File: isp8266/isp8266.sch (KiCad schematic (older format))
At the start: 70 parts, among them J1 S0, J10 9V_IN, J11 USB_C_Receptacle, J12 F1, J2 S2, J3 S1, J4 S3, J5 IMU, J6 USART, J7 F0, J8 BATTERY, J9 I2C, Q1 S8050, Q2 S8050, Q3 BSS138, Q4 IRLML6402, Q5 BSS138, Q6 IRLML6402, U1 CH340C, U2 AP1117-33, U3 IP5306, U4 ESP-12E

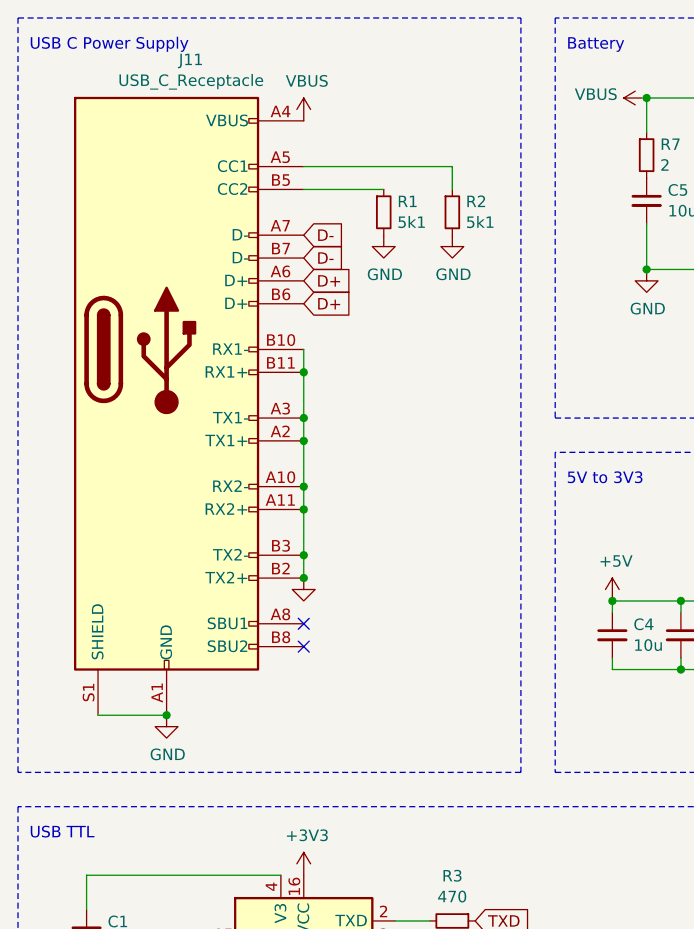
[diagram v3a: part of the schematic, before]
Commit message: Change usb c connector
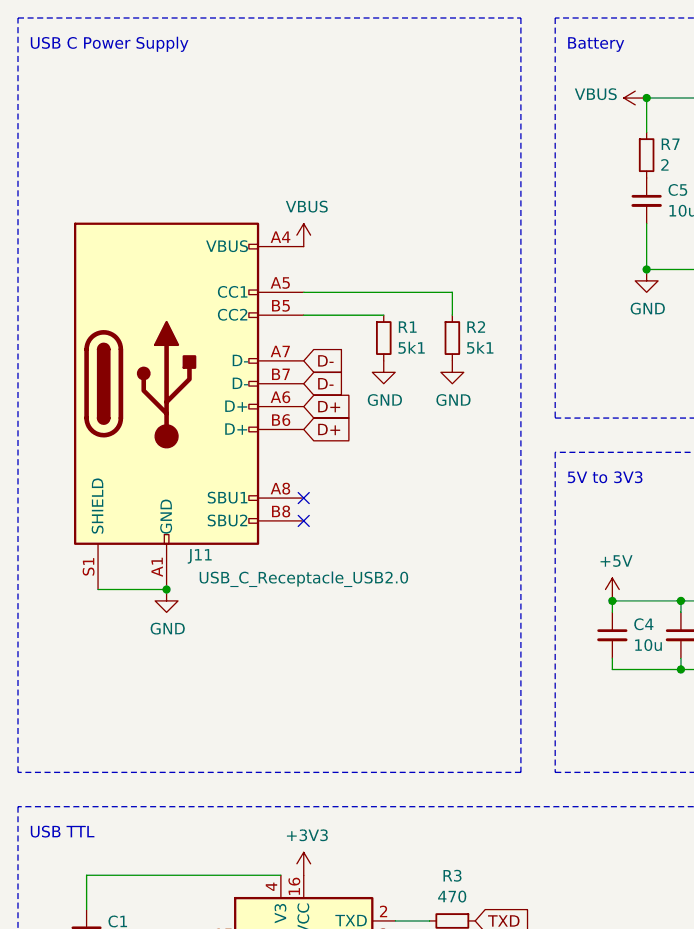
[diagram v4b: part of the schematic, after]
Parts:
- removed J11: USB_C_Receptacle, Connector_USB:USB_C_Receptacle_Amphenol_12401610E4-2A, symbol Connector:USB_C_Receptacle
- added J11: USB_C_Receptacle_USB2.0, Connector_USB:USB_C_Receptacle_Palconn_UTC16-G, symbol Connector:USB_C_Receptacle_USB2.0
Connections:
- net -BATT: now also J11.A1 (GND), J11.A12 (GND), J11.B1 (GND), J11.B12 (GND), J11.S1 (SHIELD)
- net D+: now also J11.A6 (D+), J11.B6 (D+)
- net D-: now also J11.A7 (D-), J11.B7 (D-)
- net VBUS: now also J11.A4 (VBUS), J11.A9 (VBUS), J11.B4 (VBUS), J11.B9 (VBUS)
- net at R1.1: now also J11.B5 (CC2)
- net at R2.1: now also J11.A5 (CC1)
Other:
- moved on the sheet: R1, R2
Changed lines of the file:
@@
 Comment4 ""
 $EndDescr
-Text GLabel 1900 1750 2    50   Input ~ 0
+Text GLabel 1900 2300 2    50   Input ~ 0
 D+
-Text GLabel 1900 1550 2    50   Input ~ 0
+Text GLabel 1900 2100 2    50   Input ~ 0
 D-
-Wire Wire Line
-	1000 3650 1300 3650
-$Comp
-L power:GND #PWR04
-U 1 1 638110D1
-P 1300 3650
-F 0 "#PWR04" H 1300 3400 50  0001 C CNN
-F 1 "GND" H 1305 3477 50  0000 C CNN
-F 2 "" H 1300 3650 50  0001 C CNN
-F 3 "" H 1300 3650 50  0001 C CNN
-	1    1300 3650
-	1    0    0    -1
-$EndComp
 $Comp
 L Device:R_Small R1
 U 1 1 63811A2A
-P 2250 1450
-F 0 "R1" H 2309 1496 50  0000 L CNN
-F 1 "5k1" H 2309 1405 50  0000 L CNN
-F 2 "Resistor_SMD:R_0603_1608Metric" H 2250 1450 50  0001 C CNN
-F 3 "~" H 2250 1450 50  0001 C CNN
-	1    2250 1450
+P 2250 2000
+F 0 "R1" H 2309 2046 50  0000 L CNN
+F 1 "5k1" H 2309 1955 50  0000 L CNN
+F 2 "Resistor_SMD:R_0603_1608Metric" H 2250 2000 50  0001 C CNN
+F 3 "~" H 2250 2000 50  0001 C CNN
+	1    2250 2000
 	1    0    0    -1
 $EndComp
@@
 L Device:R_Small R2
 U 1 1 63813179
-P 2550 1450
-F 0 "R2" H 2609 1496 50  0000 L CNN
-F 1 "5k1" H 2609 1405 50  0000 L CNN
-F 2 "Resistor_SMD:R_0603_1608Metric" H 2550 1450 50  0001 C CNN
-F 3 "~" H 2550 1450 50  0001 C CNN
-	1    2550 1450
-	1    0    0    -1
-$EndComp
-Wire Wire Line
-	2550 1350 2550 1250
-Wire Wire Line
-	2550 1250 1900 1250
-Wire Wire Line
-	1900 1350 2250 1350
+P 2550 2000
+F 0 "R2" H 2609 2046 50  0000 L CNN
+F 1 "5k1" H 2609 1955 50  0000 L CNN
+F 2 "Resistor_SMD:R_0603_1608Metric" H 2550 2000 50  0001 C CNN
+F 3 "~" H 2550 2000 50  0001 C CNN
+	1    2550 2000
+	1    0    0    -1
+$EndComp
+Wire Wire Line
+	2550 1900 2550 1800
+Wire Wire Line
+	2550 1800 1900 1800
+Wire Wire Line
+	1900 1900 2250 1900
 $Comp
 L power:GND #PWR09
 U 1 1 638144D3
-P 2250 1550
-F 0 "#PWR09" H 2250 1300 50  0001 C CNN
-F 1 "GND" H 2255 1377 50  0000 C CNN
-F 2 "" H 2250 1550 50  0001 C CNN
-F 3 "" H 2250 1550 50  0001 C CNN
-	1    2250 1550
+P 2250 2100
+F 0 "#PWR09" H 2250 1850 50  0001 C CNN
+F 1 "GND" H 2255 1927 50  0000 C CNN
+F 2 "" H 2250 2100 50  0001 C CNN
+F 3 "" H 2250 2100 50  0001 C CNN
+	1    2250 2100
 	1    0    0    -1
 $EndComp
@@
 L power:GND #PWR010
 U 1 1 63814BDE
-P 2550 1550
-F 0 "#PWR010" H 2550 1300 50  0001 C CNN
-F 1 "GND" H 2555 1377 50  0000 C CNN
-F 2 "" H 2550 1550 50  0001 C CNN
-F 3 "" H 2550 1550 50  0001 C CNN
-	1    2550 1550
-	1    0    0    -1
-$EndComp
-$Comp
-L power:GND #PWR06
-U 1 1 63815628
-P 1900 3050
-F 0 "#PWR06" H 1900 2800 50  0001 C CNN
-F 1 "GND" H 1905 2877 50  0001 C CNN
-F 2 "" H 1900 3050 50  0001 C CNN
-F 3 "" H 1900 3050 50  0001 C CNN
-	1    1900 3050
-	1    0    0    -1
-$EndComp
-NoConn ~ 1900 3250
-NoConn ~ 1900 3350
+P 2550 2100
+F 0 "#PWR010" H 2550 1850 50  0001 C CNN
+F 1 "GND" H 2555 1927 50  0000 C CNN
+F 2 "" H 2550 2100 50  0001 C CNN
+F 3 "" H 2550 2100 50  0001 C CNN
+	1    2550 2100
+	1    0    0    -1
+$EndComp
 $Comp
 L power:VBUS #PWR05
 U 1 1 63834DD7
-P 1900 1050
-F 0 "#PWR05" H 1900 900 50  0001 C CNN
-F 1 "VBUS" H 1915 1223 50  0000 C CNN
-F 2 "" H 1900 1050 50  0001 C CNN
-F 3 "" H 1900 1050 50  0001 C CNN
-	1    1900 1050
+P 1900 1600
+F 0 "#PWR05" H 1900 1450 50  0001 C CNN
+F 1 "VBUS" H 1915 1773 50  0000 C CNN
+F 2 "" H 1900 1600 50  0001 C CNN
+F 3 "" H 1900 1600 50  0001 C CNN
+	1    1900 1600
 	1    0    0    -1
 $EndComp
@@
 	1    0    0    -1
 $EndComp
-$Comp
-L Connector:USB_C_Receptacle J11
-U 1 1 63C95E22
-P 1300 2050
-F 0 "J11" H 1407 3317 50  0000 C CNN
-F 1 "USB_C_Receptacle" H 1407 3226 50  0000 C CNN
-F 2 "Connector_USB:USB_C_Receptacle_Amphenol_12401610E4-2A" H 1450 2050 50  0001 C CNN
-F 3 "https://www.usb.org/sites/default/files/documents/usb_type-c.zip" H 1450 2050 50  0001 C CNN
-	1    1300 2050
-	1    0    0    -1
-$EndComp
-Connection ~ 1300 3650
-Wire Wire Line
-	1900 2950 1900 3050
-Connection ~ 1900 3050
-Wire Wire Line
-	1900 2050 1900 2150
-Connection ~ 1900 2150
-Wire Wire Line
-	1900 2150 1900 2350
-Connection ~ 1900 2350
-Wire Wire Line
-	1900 2350 1900 2450
-Connection ~ 1900 2450
-Wire Wire Line
-	1900 2450 1900 2650
-Connection ~ 1900 2650
-Wire Wire Line
-	1900 2650 1900 2750
-Connection ~ 1900 2750
-Wire Wire Line
-	1900 2750 1900 2950
-Connection ~ 1900 2950
-Text GLabel 1900 1650 2    50   Input ~ 0
-D-
-Text GLabel 1900 1850 2    50   Input ~ 0
-D+
 Wire Notes Line
 	3000 3900 5650 3900
@@
 $EndComp
 Connection ~ 8850 5050
+Text GLabel 1900 2400 2    50   Input ~ 0
+D+
+Text GLabel 1900 2200 2    50   Input ~ 0
+D-
+Wire Wire Line
+	1000 3100 1300 3100
+$Comp
+L power:GND #PWR04
+U 1 1 638110D1
+P 1300 3100
+F 0 "#PWR04" H 1300 2850 50  0001 C CNN
+F 1 "GND" H 1305 2927 50  0000 C CNN
+F 2 "" H 1300 3100 50  0001 C CNN
+F 3 "" H 1300 3100 50  0001 C CNN
+	1    1300 3100
+	1    0    0    -1
+$EndComp
+Connection ~ 1300 3100
+$Comp
+L Connector:USB_C_Receptacle_USB2.0 J11
+U 1 1 63983D7F
+P 1300 2200
+F 0 "J11" H 1450 1450 50  0000 C CNN
+F 1 "USB_C_Receptacle_USB2.0" H 1900 1350 50  0000 C CNN
+F 2 "Connector_USB:USB_C_Receptacle_Palconn_UTC16-G" H 1450 2200 50  0001 C CNN
+F 3 "https://www.usb.org/sites/default/files/documents/usb_type-c.zip" H 1450 2200 50  0001 C CNN
+	1    1300 2200
+	1    0    0    -1
+$EndComp
+NoConn ~ 1900 2800
+NoConn ~ 1900 2700
 $EndSCHEMATC

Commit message: Edit BJT footprint
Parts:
- Q1, Q2: footprint Package_TO_SOT_THT:TO-92_Inline -> Package_TO_SOT_SMD:SOT-23
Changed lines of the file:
@@
 F 0 "Q1" H 3541 5046 50  0000 L CNN
 F 1 "S8050" H 3541 4955 50  0000 L CNN
-F 2 "Package_TO_SOT_THT:TO-92_Inline" H 3550 4925 50  0001 L CIN
+F 2 "Package_TO_SOT_SMD:SOT-23" H 3550 4925 50  0001 L CIN
 F 3 "http://www.unisonic.com.tw/datasheet/S8050.pdf" H 3350 5000 50  0001 L CNN
 	1    3350 5000
@@
 F 0 "Q2" H 3541 5404 50  0000 L CNN
 F 1 "S8050" H 3541 5495 50  0000 L CNN
-F 2 "Package_TO_SOT_THT:TO-92_Inline" H 3550 5375 50  0001 L CIN
+F 2 "Package_TO_SOT_SMD:SOT-23" H 3550 5375 50  0001 L CIN
 F 3 "http://www.unisonic.com.tw/datasheet/S8050.pdf" H 3350 5450 50  0001 L CNN
 	1    3350 5450

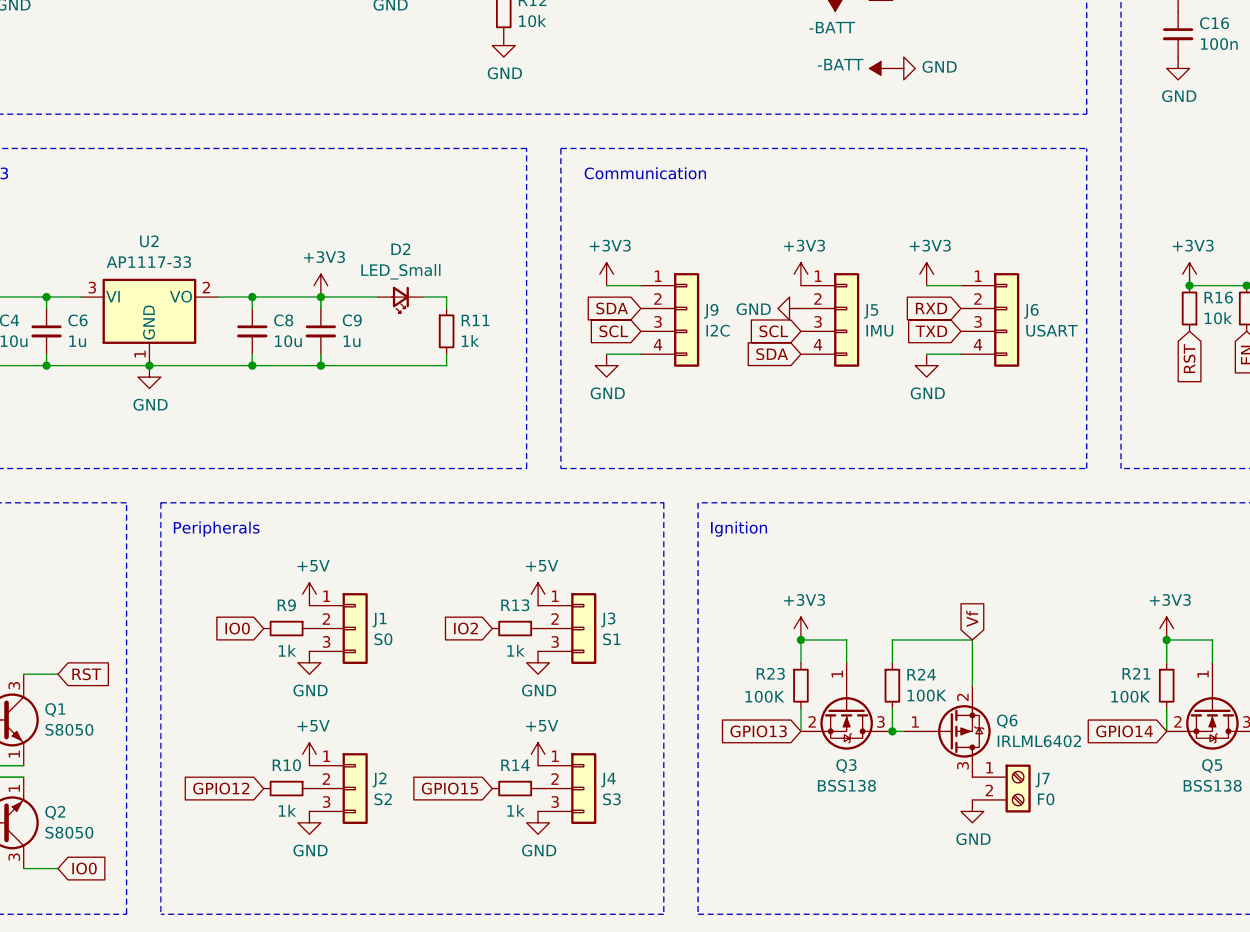
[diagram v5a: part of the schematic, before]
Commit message: Change pinout connector
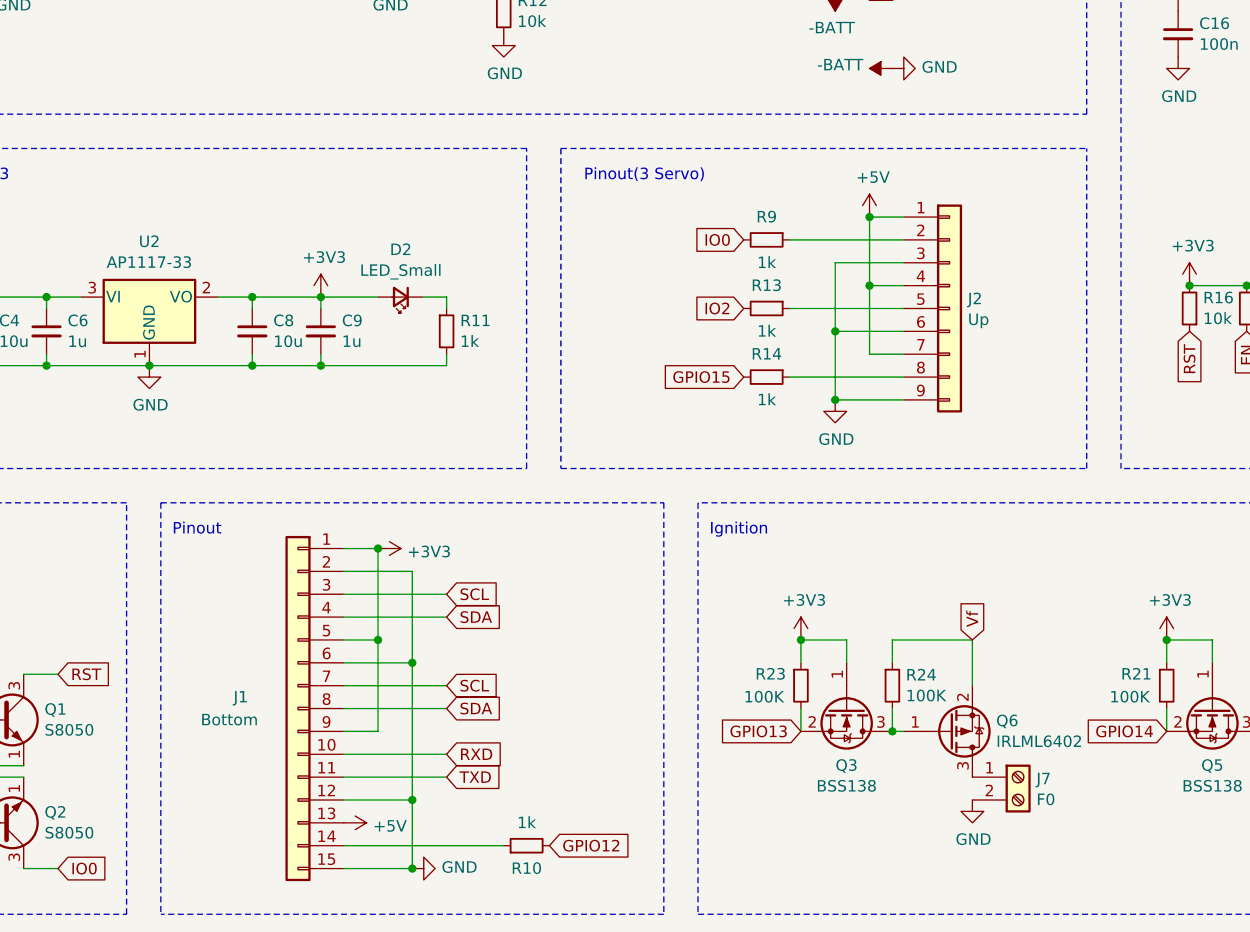
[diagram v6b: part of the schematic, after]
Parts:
- removed J1: S0, Connector_PinSocket_2.54mm:PinSocket_1x03_P2.54mm_Vertical, symbol Connector_Generic:Conn_01x03
- removed J2: S2, Connector_PinSocket_2.54mm:PinSocket_1x03_P2.54mm_Vertical, symbol Connector_Generic:Conn_01x03
- removed J3: S1, Connector_PinSocket_2.54mm:PinSocket_1x03_P2.54mm_Vertical, symbol Connector_Generic:Conn_01x03
- removed J4: S3, Connector_PinSocket_2.54mm:PinSocket_1x03_P2.54mm_Vertical, symbol Connector_Generic:Conn_01x03
- removed J5: IMU, Connector_PinSocket_2.54mm:PinSocket_1x04_P2.54mm_Vertical, symbol Connector_Generic:Conn_01x04
- removed J6: USART, Connector_PinSocket_2.54mm:PinSocket_1x04_P2.54mm_Vertical, symbol Connector_Generic:Conn_01x04
- removed J9: I2C, Connector_PinSocket_2.54mm:PinSocket_1x04_P2.54mm_Vertical, symbol Connector_Generic:Conn_01x04
- added J1: Bottom, Connector_PinHeader_2.54mm:PinHeader_1x15_P2.54mm_Vertical, symbol Connector_Generic:Conn_01x15
- added J2: Up, Connector_PinHeader_2.54mm:PinHeader_1x09_P2.54mm_Vertical, symbol Connector_Generic:Conn_01x09
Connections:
- net +3V3: now also J1.1 (Pin_1), J1.5 (Pin_5), J1.9 (Pin_9)
- net +5V: now also J1.13 (Pin_13), J2.1 (Pin_1), J2.4 (Pin_4), J2.7 (Pin_7)
- net -BATT: now also J1.12 (Pin_12), J1.15 (Pin_15), J1.2 (Pin_2), J1.6 (Pin_6), J2.3 (Pin_3), J2.6 (Pin_6), J2.9 (Pin_9)
- net RXD: now also J1.10 (Pin_10)
- net SCL: now also J1.3 (Pin_3), J1.7 (Pin_7)
- net SDA: now also J1.4 (Pin_4), J1.8 (Pin_8)
- net TXD: now also J1.11 (Pin_11)
- net at R9.1: now also J2.2 (Pin_2)
- net at R13.1: now also J2.5 (Pin_5)
- net at R10.1: now also J1.14 (Pin_14)
- net at R14.1: now also J2.8 (Pin_8)
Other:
- note added: "Pinout"
- note added: "Pinout(3 Servo)"
- note removed: "Communication"
- note removed: "Peripherals"
- moved on the sheet: R10, R13, R14, R9

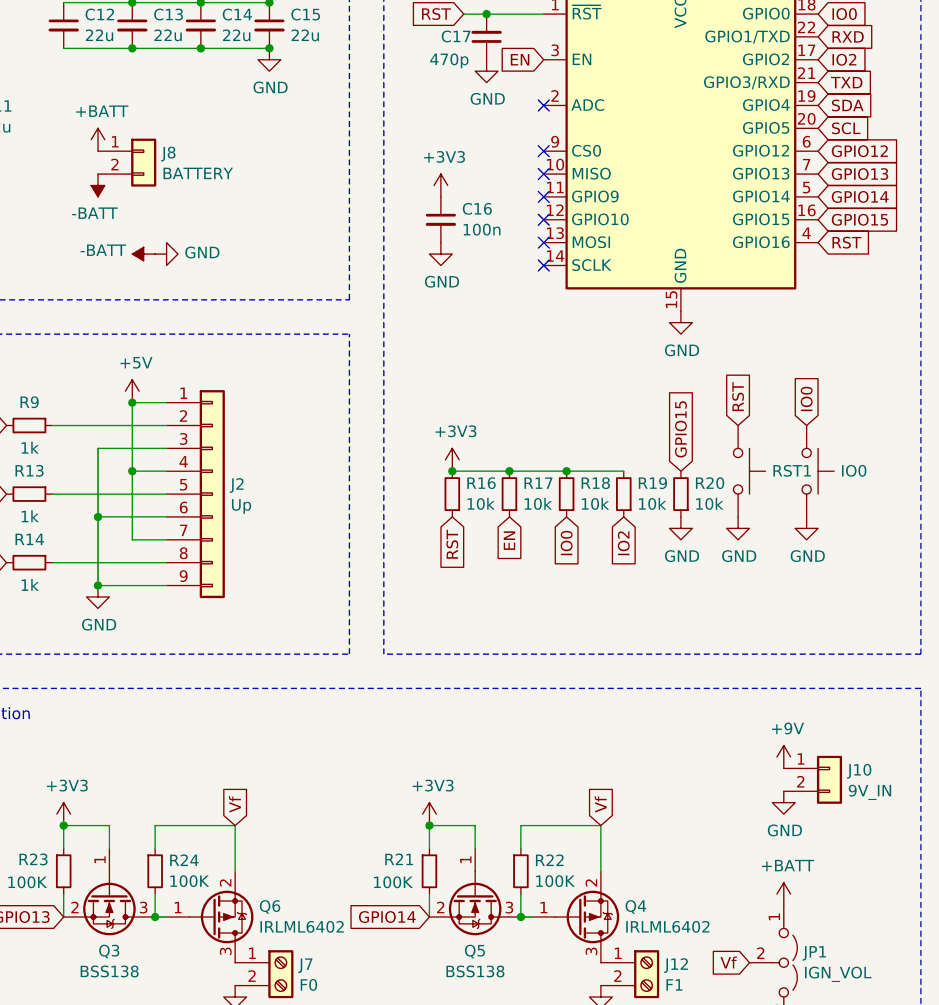
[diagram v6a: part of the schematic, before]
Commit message: Connect battery in series
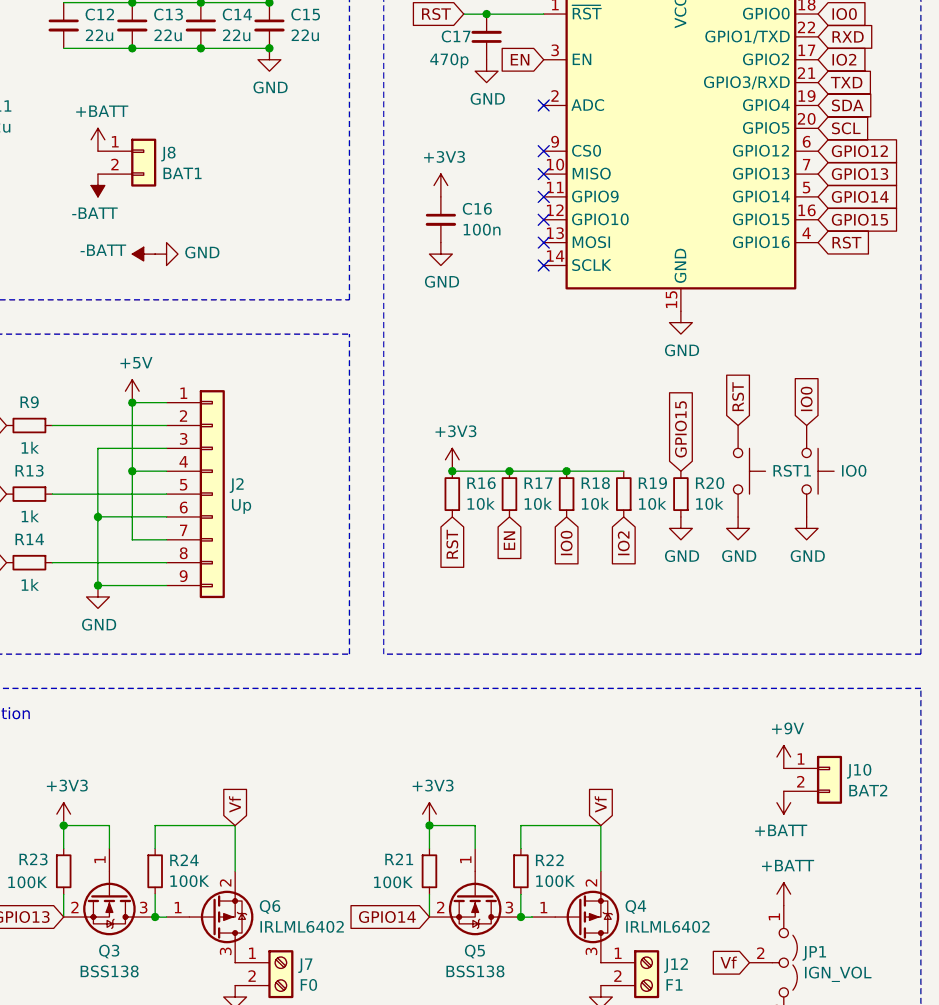
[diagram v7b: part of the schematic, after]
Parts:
- J10: value 9V_IN -> BAT2
- J8: value BATTERY -> BAT1
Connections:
- net +BATT: now also J10.2 (Pin_2)
- net -BATT: no longer J10.2 (Pin_2)
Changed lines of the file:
@@
 P 7200 1700
 F 0 "J8" H 7280 1692 50  0000 L CNN
-F 1 "BATTERY" H 7280 1601 50  0000 L CNN
+F 1 "BAT1" H 7280 1601 50  0000 L CNN
 F 2 "Connector_Molex:Molex_KK-254_AE-6410-02A_1x02_P2.54mm_Vertical" H 7200 1700 50  0001 C CNN
 F 3 "~" H 7200 1700 50  0001 C CNN
@@
 	1    0    0    -1
 $EndComp
-$Comp
-L Device:C_Small C17
-U 1 1 6392BA1B
-P 8700 1200
-F 0 "C17" H 8900 1200 50  0000 R CNN
-F 1 "470p" H 8950 1300 50  0000 R CNN
-F 2 "Capacitor_SMD:C_0603_1608Metric" H 8700 1200 50  0001 C CNN
-F 3 "~" H 8700 1200 50  0001 C CNN
-	1    8700 1200
-	-1   0    0    1
-$EndComp
 Text GLabel 8600 1100 0    50   Input ~ 0
 RST
@@
 P 10200 4400
 F 0 "J10" H 10280 4392 50  0000 L CNN
-F 1 "9V_IN" H 10280 4301 50  0000 L CNN
+F 1 "BAT2" H 10280 4301 50  0000 L CNN
 F 2 "Connector_Molex:Molex_KK-254_AE-6410-02A_1x02_P2.54mm_Vertical" H 10200 4400 50  0001 C CNN
 F 3 "~" H 10200 4400 50  0001 C CNN
 	1    10200 4400
-	1    0    0    -1
-$EndComp
-$Comp
-L power:GND #PWR057
-U 1 1 63958BCC
-P 10000 4500
-F 0 "#PWR057" H 10000 4250 50  0001 C CNN
-F 1 "GND" H 10005 4327 50  0000 C CNN
-F 2 "" H 10000 4500 50  0001 C CNN
-F 3 "" H 10000 4500 50  0001 C CNN
-	1    10000 4500
 	1    0    0    -1
 $EndComp
@@
 	4850 5650 5150 5650
 $Comp
-L power:+5V #PWR?
+L power:+5V #PWR0105
 U 1 1 639AAB33
 P 7150 2800
-F 0 "#PWR?" H 7150 2650 50  0001 C CNN
+F 0 "#PWR0105" H 7150 2650 50  0001 C CNN
 F 1 "+5V" H 7165 2973 50  0000 C CNN
 F 2 "" H 7150 2800 50  0001 C CNN
@@
 $EndComp
 Connection ~ 7150 2800
+$Comp
+L Device:C_Small C17
+U 1 1 6392BA1B
+P 8700 1200
+F 0 "C17" H 8900 1200 50  0000 R CNN
+F 1 "470p" H 8950 1300 50  0000 R CNN
+F 2 "Capacitor_SMD:C_0603_1608Metric" H 8700 1200 50  0001 C CNN
+F 3 "~" H 8700 1200 50  0001 C CNN
+	1    8700 1200
+	-1   0    0    1
+$EndComp
+$Comp
+L power:+BATT #PWR?
+U 1 1 63A6D1A8
+P 10000 4500
+F 0 "#PWR?" H 10000 4350 50  0001 C CNN
+F 1 "+BATT" H 10015 4673 50  0000 C CNN
+F 2 "" H 10000 4500 50  0001 C CNN
+F 3 "" H 10000 4500 50  0001 C CNN
+	1    10000 4500
+	-1   0    0    1
+$EndComp
 $EndSCHEMATC
